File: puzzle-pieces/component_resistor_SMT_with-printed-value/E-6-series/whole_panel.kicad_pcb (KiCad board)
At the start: 2 copper layers, 200 x 200 mm, 175 parts, among them J1 Conn_01x02_Pin, J10 Conn_01x02_Pin, J11 Conn_01x02_Pin, J12 Conn_01x02_Pin, J13 Conn_01x02_Pin, J14 Conn_01x02_Pin, J15 Conn_01x02_Pin, J16 Conn_01x02_Pin, J17 Conn_01x02_Pin, J18 Conn_01x02_Pin, J19 Conn_01x02_Pin, J2 Conn_01x02_Pin, J20 Conn_01x02_Pin, J21 Conn_01x02_Pin, J22 Conn_01x02_Pin, J23 Conn_01x02_Pin, J24 Conn_01x02_Pin, J25 Conn_01x02_Pin, J26 Conn_01x02_Pin, J27 Conn_01x02_Pin, J28 Conn_01x02_Pin, J29 Conn_01x02_Pin, J3 Conn_01x02_Pin, J30 Conn_01x02_Pin, J31 Conn_01x02_Pin, J32 Conn_01x02_Pin, J33 Conn_01x02_Pin, J34 Conn_01x02_Pin, J35 Conn_01x02_Pin, J36 Conn_01x02_Pin, J37 Conn_01x02_Pin, J38 Conn_01x02_Pin, J39 Conn_01x02_Pin, J4 Conn_01x02_Pin, J40 Conn_01x02_Pin, J41 Conn_01x02_Pin, J42 Conn_01x02_Pin, J43 Conn_01x02_Pin, J44 Conn_01x02_Pin, J45 Conn_01x02_Pin, J46 Conn_01x02_Pin, J47 Conn_01x02_Pin, J48 Conn_01x02_Pin, J49 Conn_01x02_Pin, J5 Conn_01x02_Pin, J50 Conn_01x02_Pin, J6 Conn_01x02_Pin, J7 Conn_01x02_Pin, J8 Conn_01x02_Pin, J9 Conn_01x02_Pin

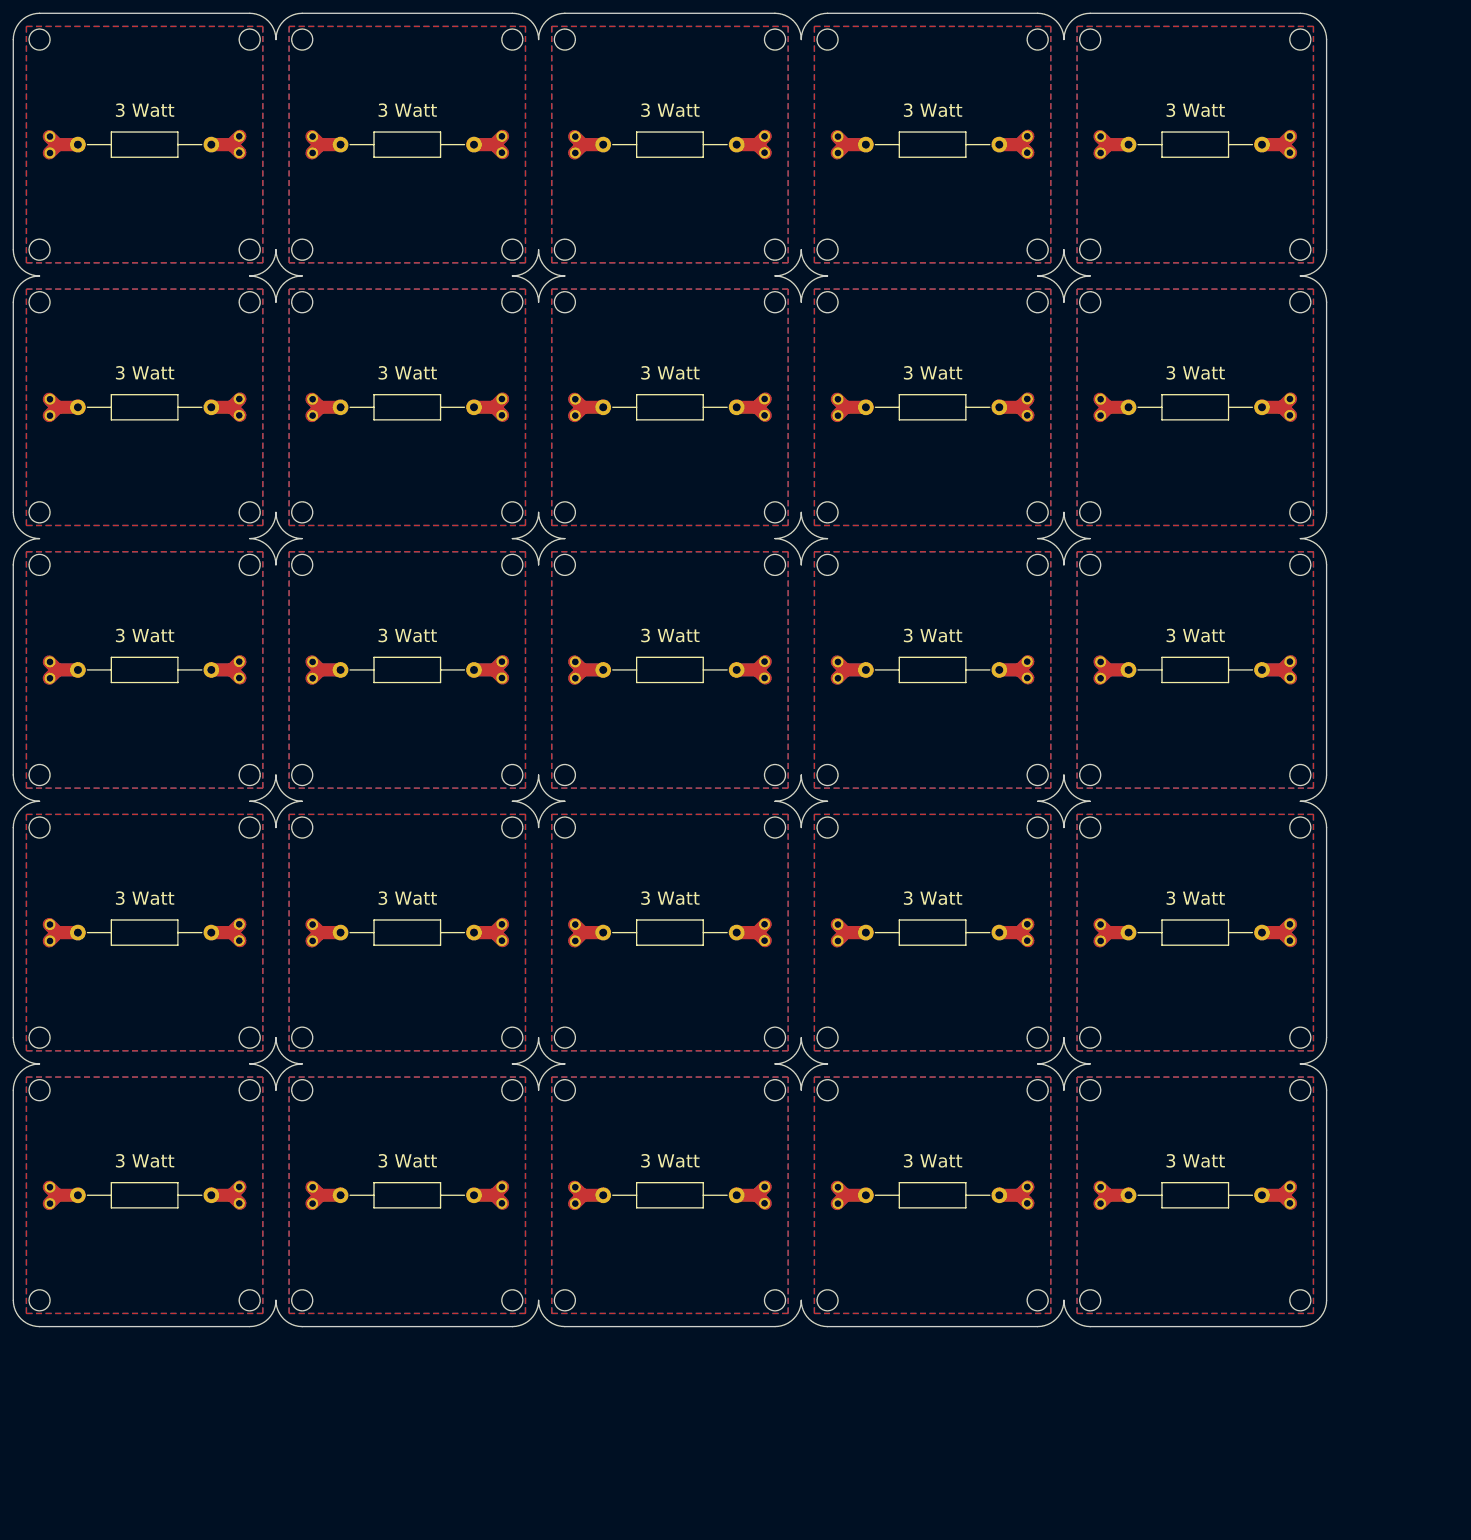
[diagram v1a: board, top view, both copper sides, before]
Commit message: Update resistor footprints and add THT 3W production files
Replaced mounting hole footprints with SMD resistor footprints in the SMT E-6 series panel and updated net assignments. Added new KiCad PCB, project, and production ZIP files for the THT 3W E-6 series resistors. Updated connector reference and position in the SMT panel.
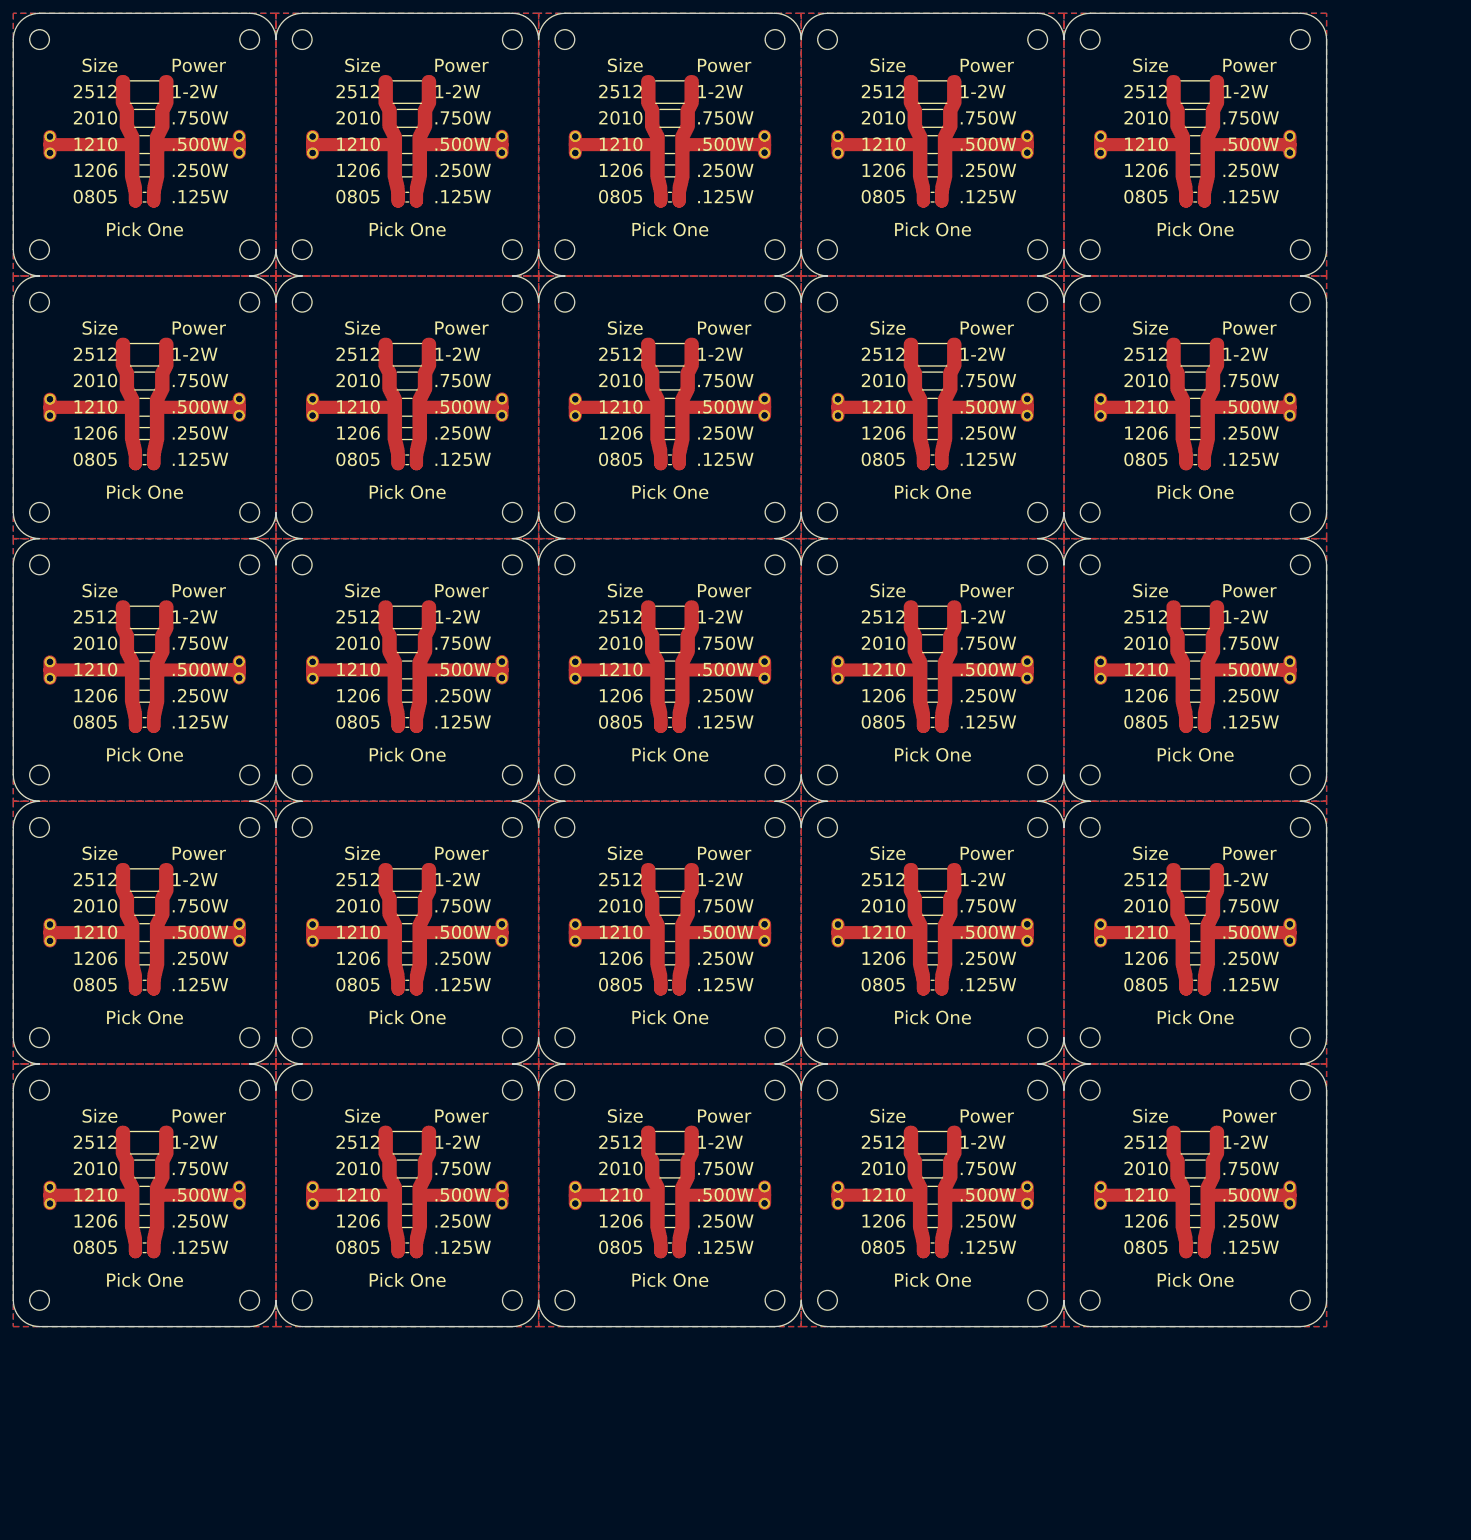
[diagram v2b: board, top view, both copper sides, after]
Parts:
- removed H5 (x100): MH M3, MountingHole:MountingHole_3.2mm_M3
- removed the J1 at (194.5, 180.0)
- removed J10, J11, J12, J13, J14, J15, J16, J17, J18, J19, J20, J21, J22, J23, J24, J25, J26, J27, J28, J29, J3, J30, J31, J32, J33, J34, J35, J36, J37, J38, J39, J4, J40, J41, J42, J43, J44, J45, J46, J47, J48, J49, J5, J50, J6, J7, J8, J9: Conn_01x02_Pin, EASYEDA2KICAD:Magentic_Connector_1x02_P2.5mm_Horizontal
- removed the R1 at (190.2, 180.0)
- removed R10, R11, R12, R13, R14, R15, R16, R17, R18, R19, R20, R21, R22, R23, R24, R25, R6, R7, R8, R9: R, Resistor_THT:R_Axial_DIN0411_L9.9mm_D3.6mm_P20.32mm_Horizontal
- removed the R2 at (30.2, 20.0)
- removed the R3 at (70.2, 20.0)
- removed the R4 at (110.2, 20.0)
- removed the R5 at (150.2, 20.0)
- added H1: MH M3, EASYEDA2KICAD:MountingHole_3.0mm_M3_tight, F.Cu at (156.0, 124.0)
- added H1: MH M3, EASYEDA2KICAD:MountingHole_3.0mm_M3_tight, F.Cu at (156.0, 164.0)
- added H1: MH M3, EASYEDA2KICAD:MountingHole_3.0mm_M3_tight, F.Cu at (116.0, 164.0)
- added H1: MH M3, EASYEDA2KICAD:MountingHole_3.0mm_M3_tight, F.Cu at (76.0, 124.0)
- added H1: MH M3, EASYEDA2KICAD:MountingHole_3.0mm_M3_tight, F.Cu at (76.0, 4.00)
- added H1: MH M3, EASYEDA2KICAD:MountingHole_3.0mm_M3_tight, F.Cu at (36.0, 84.0)
- added H1: MH M3, EASYEDA2KICAD:MountingHole_3.0mm_M3_tight, F.Cu at (36.0, 44.0)
- added H1: MH M3, EASYEDA2KICAD:MountingHole_3.0mm_M3_tight, F.Cu at (156.0, 44.0)
- added H1: MH M3, EASYEDA2KICAD:MountingHole_3.0mm_M3_tight, F.Cu at (196.0, 4.00)
- added H1: MH M3, EASYEDA2KICAD:MountingHole_3.0mm_M3_tight, F.Cu at (196.0, 124.0)
- added H1: MH M3, EASYEDA2KICAD:MountingHole_3.0mm_M3_tight, F.Cu at (196.0, 44.0)
- added H1: MH M3, EASYEDA2KICAD:MountingHole_3.0mm_M3_tight, F.Cu at (116.0, 44.0)
- added H1: MH M3, EASYEDA2KICAD:MountingHole_3.0mm_M3_tight, F.Cu at (116.0, 4.00)
- added H1: MH M3, EASYEDA2KICAD:MountingHole_3.0mm_M3_tight, F.Cu at (156.0, 84.0)
- added H1: MH M3, EASYEDA2KICAD:MountingHole_3.0mm_M3_tight, F.Cu at (116.0, 84.0)
- added H1: MH M3, EASYEDA2KICAD:MountingHole_3.0mm_M3_tight, F.Cu at (196.0, 84.0)
- added H1: MH M3, EASYEDA2KICAD:MountingHole_3.0mm_M3_tight, F.Cu at (196.0, 164.0)
- added H1: MH M3, EASYEDA2KICAD:MountingHole_3.0mm_M3_tight, F.Cu at (156.0, 4.00)
- added H1: MH M3, EASYEDA2KICAD:MountingHole_3.0mm_M3_tight, F.Cu at (116.0, 124.0)
- added H1: MH M3, EASYEDA2KICAD:MountingHole_3.0mm_M3_tight, F.Cu at (76.0, 84.0)
- added H1: MH M3, EASYEDA2KICAD:MountingHole_3.0mm_M3_tight, F.Cu at (36.0, 124.0)
- added H1: MH M3, EASYEDA2KICAD:MountingHole_3.0mm_M3_tight, F.Cu at (76.0, 44.0)
- added H1: MH M3, EASYEDA2KICAD:MountingHole_3.0mm_M3_tight, F.Cu at (76.0, 164.0)
- added H1: MH M3, EASYEDA2KICAD:MountingHole_3.0mm_M3_tight, F.Cu at (36.0, 4.00)
- added H1: MH M3, EASYEDA2KICAD:MountingHole_3.0mm_M3_tight, F.Cu at (36.0, 164.0)
- added H2: MH M3, EASYEDA2KICAD:MountingHole_3.0mm_M3_tight, F.Cu at (4.00, 84.0)
- added H2: MH M3, EASYEDA2KICAD:MountingHole_3.0mm_M3_tight, F.Cu at (124.0, 4.00)
- added H2: MH M3, EASYEDA2KICAD:MountingHole_3.0mm_M3_tight, F.Cu at (124.0, 164.0)
- added H2: MH M3, EASYEDA2KICAD:MountingHole_3.0mm_M3_tight, F.Cu at (124.0, 124.0)
- added H2: MH M3, EASYEDA2KICAD:MountingHole_3.0mm_M3_tight, F.Cu at (164.0, 44.0)
- added H2: MH M3, EASYEDA2KICAD:MountingHole_3.0mm_M3_tight, F.Cu at (84.0, 84.0)
- added H2: MH M3, EASYEDA2KICAD:MountingHole_3.0mm_M3_tight, F.Cu at (84.0, 4.00)
- added H2: MH M3, EASYEDA2KICAD:MountingHole_3.0mm_M3_tight, F.Cu at (44.0, 124.0)
- added H2: MH M3, EASYEDA2KICAD:MountingHole_3.0mm_M3_tight, F.Cu at (44.0, 44.0)
- added H2: MH M3, EASYEDA2KICAD:MountingHole_3.0mm_M3_tight, F.Cu at (44.0, 84.0)
- added H2: MH M3, EASYEDA2KICAD:MountingHole_3.0mm_M3_tight, F.Cu at (84.0, 124.0)
- added H2: MH M3, EASYEDA2KICAD:MountingHole_3.0mm_M3_tight, F.Cu at (4.00, 4.00)
- added H2: MH M3, EASYEDA2KICAD:MountingHole_3.0mm_M3_tight, F.Cu at (124.0, 84.0)
- added H2: MH M3, EASYEDA2KICAD:MountingHole_3.0mm_M3_tight, F.Cu at (124.0, 44.0)
- added H2: MH M3, EASYEDA2KICAD:MountingHole_3.0mm_M3_tight, F.Cu at (4.00, 124.0)
- added H2: MH M3, EASYEDA2KICAD:MountingHole_3.0mm_M3_tight, F.Cu at (164.0, 164.0)
- added H2: MH M3, EASYEDA2KICAD:MountingHole_3.0mm_M3_tight, F.Cu at (4.00, 44.0)
- added H2: MH M3, EASYEDA2KICAD:MountingHole_3.0mm_M3_tight, F.Cu at (164.0, 4.00)
- added H2: MH M3, EASYEDA2KICAD:MountingHole_3.0mm_M3_tight, F.Cu at (164.0, 124.0)
- added H2: MH M3, EASYEDA2KICAD:MountingHole_3.0mm_M3_tight, F.Cu at (84.0, 164.0)
- added H2: MH M3, EASYEDA2KICAD:MountingHole_3.0mm_M3_tight, F.Cu at (84.0, 44.0)
- added H2: MH M3, EASYEDA2KICAD:MountingHole_3.0mm_M3_tight, F.Cu at (164.0, 84.0)
- added H2: MH M3, EASYEDA2KICAD:MountingHole_3.0mm_M3_tight, F.Cu at (4.00, 164.0)
- added H2: MH M3, EASYEDA2KICAD:MountingHole_3.0mm_M3_tight, F.Cu at (44.0, 4.00)
- added H2: MH M3, EASYEDA2KICAD:MountingHole_3.0mm_M3_tight, F.Cu at (44.0, 164.0)
- added H3: MH M3, EASYEDA2KICAD:MountingHole_3.0mm_M3_tight, F.Cu at (156.0, 156.0)
- added H3: MH M3, EASYEDA2KICAD:MountingHole_3.0mm_M3_tight, F.Cu at (156.0, 116.0)
- added H3: MH M3, EASYEDA2KICAD:MountingHole_3.0mm_M3_tight, F.Cu at (196.0, 76.0)
- added H3: MH M3, EASYEDA2KICAD:MountingHole_3.0mm_M3_tight, F.Cu at (36.0, 116.0)
- added H3: MH M3, EASYEDA2KICAD:MountingHole_3.0mm_M3_tight, F.Cu at (76.0, 36.0)
- added H3: MH M3, EASYEDA2KICAD:MountingHole_3.0mm_M3_tight, F.Cu at (36.0, 76.0)
- added H3: MH M3, EASYEDA2KICAD:MountingHole_3.0mm_M3_tight, F.Cu at (196.0, 116.0)
- added H3: MH M3, EASYEDA2KICAD:MountingHole_3.0mm_M3_tight, F.Cu at (116.0, 36.0)
- added H3: MH M3, EASYEDA2KICAD:MountingHole_3.0mm_M3_tight, F.Cu at (116.0, 116.0)
- added H3: MH M3, EASYEDA2KICAD:MountingHole_3.0mm_M3_tight, F.Cu at (36.0, 36.0)
- added H3: MH M3, EASYEDA2KICAD:MountingHole_3.0mm_M3_tight, F.Cu at (156.0, 196.0)
- added H3: MH M3, EASYEDA2KICAD:MountingHole_3.0mm_M3_tight, F.Cu at (196.0, 36.0)
- added H3: MH M3, EASYEDA2KICAD:MountingHole_3.0mm_M3_tight, F.Cu at (76.0, 156.0)
- added H3: MH M3, EASYEDA2KICAD:MountingHole_3.0mm_M3_tight, F.Cu at (76.0, 196.0)
- added H3: MH M3, EASYEDA2KICAD:MountingHole_3.0mm_M3_tight, F.Cu at (196.0, 196.0)
- added H3: MH M3, EASYEDA2KICAD:MountingHole_3.0mm_M3_tight, F.Cu at (76.0, 76.0)
- added H3: MH M3, EASYEDA2KICAD:MountingHole_3.0mm_M3_tight, F.Cu at (116.0, 156.0)
- added H3: MH M3, EASYEDA2KICAD:MountingHole_3.0mm_M3_tight, F.Cu at (36.0, 196.0)
- added H3: MH M3, EASYEDA2KICAD:MountingHole_3.0mm_M3_tight, F.Cu at (116.0, 76.0)
- added H3: MH M3, EASYEDA2KICAD:MountingHole_3.0mm_M3_tight, F.Cu at (156.0, 76.0)
- added H3: MH M3, EASYEDA2KICAD:MountingHole_3.0mm_M3_tight, F.Cu at (116.0, 196.0)
- added H3: MH M3, EASYEDA2KICAD:MountingHole_3.0mm_M3_tight, F.Cu at (36.0, 156.0)
- added H3: MH M3, EASYEDA2KICAD:MountingHole_3.0mm_M3_tight, F.Cu at (76.0, 116.0)
- added H3: MH M3, EASYEDA2KICAD:MountingHole_3.0mm_M3_tight, F.Cu at (196.0, 156.0)
- added H3: MH M3, EASYEDA2KICAD:MountingHole_3.0mm_M3_tight, F.Cu at (156.0, 36.0)
- added H4: MH M3, EASYEDA2KICAD:MountingHole_3.0mm_M3_tight, F.Cu at (84.0, 196.0)
- added H4: MH M3, EASYEDA2KICAD:MountingHole_3.0mm_M3_tight, F.Cu at (44.0, 196.0)
- added H4: MH M3, EASYEDA2KICAD:MountingHole_3.0mm_M3_tight, F.Cu at (4.00, 76.0)
- added H4: MH M3, EASYEDA2KICAD:MountingHole_3.0mm_M3_tight, F.Cu at (124.0, 196.0)
- added H4: MH M3, EASYEDA2KICAD:MountingHole_3.0mm_M3_tight, F.Cu at (84.0, 76.0)
- added H4: MH M3, EASYEDA2KICAD:MountingHole_3.0mm_M3_tight, F.Cu at (124.0, 116.0)
- added H4: MH M3, EASYEDA2KICAD:MountingHole_3.0mm_M3_tight, F.Cu at (84.0, 116.0)
- added H4: MH M3, EASYEDA2KICAD:MountingHole_3.0mm_M3_tight, F.Cu at (4.00, 156.0)
- added H4: MH M3, EASYEDA2KICAD:MountingHole_3.0mm_M3_tight, F.Cu at (124.0, 36.0)
- added H4: MH M3, EASYEDA2KICAD:MountingHole_3.0mm_M3_tight, F.Cu at (164.0, 156.0)
- added H4: MH M3, EASYEDA2KICAD:MountingHole_3.0mm_M3_tight, F.Cu at (84.0, 36.0)
- added H4: MH M3, EASYEDA2KICAD:MountingHole_3.0mm_M3_tight, F.Cu at (164.0, 36.0)
- added H4: MH M3, EASYEDA2KICAD:MountingHole_3.0mm_M3_tight, F.Cu at (164.0, 196.0)
- added H4: MH M3, EASYEDA2KICAD:MountingHole_3.0mm_M3_tight, F.Cu at (164.0, 116.0)
- added H4: MH M3, EASYEDA2KICAD:MountingHole_3.0mm_M3_tight, F.Cu at (4.00, 36.0)
- added H4: MH M3, EASYEDA2KICAD:MountingHole_3.0mm_M3_tight, F.Cu at (84.0, 156.0)
- added H4: MH M3, EASYEDA2KICAD:MountingHole_3.0mm_M3_tight, F.Cu at (44.0, 116.0)
- added H4: MH M3, EASYEDA2KICAD:MountingHole_3.0mm_M3_tight, F.Cu at (4.00, 116.0)
- added H4: MH M3, EASYEDA2KICAD:MountingHole_3.0mm_M3_tight, F.Cu at (124.0, 76.0)
- added H4: MH M3, EASYEDA2KICAD:MountingHole_3.0mm_M3_tight, F.Cu at (124.0, 156.0)
- added H4: MH M3, EASYEDA2KICAD:MountingHole_3.0mm_M3_tight, F.Cu at (4.00, 196.0)
- added H4: MH M3, EASYEDA2KICAD:MountingHole_3.0mm_M3_tight, F.Cu at (44.0, 156.0)
- added H4: MH M3, EASYEDA2KICAD:MountingHole_3.0mm_M3_tight, F.Cu at (44.0, 36.0)
- added H4: MH M3, EASYEDA2KICAD:MountingHole_3.0mm_M3_tight, F.Cu at (44.0, 76.0)
- added H4: MH M3, EASYEDA2KICAD:MountingHole_3.0mm_M3_tight, F.Cu at (164.0, 76.0)
- added J1: Conn_01x02_Pin, EASYEDA2KICAD:Magentic_Connector_1x02_P2.5mm_Horizontal, F.Cu at (45.5, 60.0)
- added J1: Conn_01x02_Pin, EASYEDA2KICAD:Magentic_Connector_1x02_P2.5mm_Horizontal, F.Cu at (5.49, 180.0)
- added J1: Conn_01x02_Pin, EASYEDA2KICAD:Magentic_Connector_1x02_P2.5mm_Horizontal, F.Cu at (125.5, 100.0)
- added J1: Conn_01x02_Pin, EASYEDA2KICAD:Magentic_Connector_1x02_P2.5mm_Horizontal, F.Cu at (165.5, 20.0)
- added J1: Conn_01x02_Pin, EASYEDA2KICAD:Magentic_Connector_1x02_P2.5mm_Horizontal, F.Cu at (45.5, 20.0)
- added J1: Conn_01x02_Pin, EASYEDA2KICAD:Magentic_Connector_1x02_P2.5mm_Horizontal, F.Cu at (85.5, 180.0)
- added J1: Conn_01x02_Pin, EASYEDA2KICAD:Magentic_Connector_1x02_P2.5mm_Horizontal, F.Cu at (45.5, 180.0)
- added J1: Conn_01x02_Pin, EASYEDA2KICAD:Magentic_Connector_1x02_P2.5mm_Horizontal, F.Cu at (5.49, 60.0)
- added J1: Conn_01x02_Pin, EASYEDA2KICAD:Magentic_Connector_1x02_P2.5mm_Horizontal, F.Cu at (85.5, 140.0)
- added J1: Conn_01x02_Pin, EASYEDA2KICAD:Magentic_Connector_1x02_P2.5mm_Horizontal, F.Cu at (85.5, 20.0)
- added J1: Conn_01x02_Pin, EASYEDA2KICAD:Magentic_Connector_1x02_P2.5mm_Horizontal, F.Cu at (165.5, 180.0)
- added J1: Conn_01x02_Pin, EASYEDA2KICAD:Magentic_Connector_1x02_P2.5mm_Horizontal, F.Cu at (165.5, 100.0)
- added J1: Conn_01x02_Pin, EASYEDA2KICAD:Magentic_Connector_1x02_P2.5mm_Horizontal, F.Cu at (125.5, 180.0)
- added J1: Conn_01x02_Pin, EASYEDA2KICAD:Magentic_Connector_1x02_P2.5mm_Horizontal, F.Cu at (85.5, 100.0)
- added J1: Conn_01x02_Pin, EASYEDA2KICAD:Magentic_Connector_1x02_P2.5mm_Horizontal, F.Cu at (45.5, 100.0)
- added J1: Conn_01x02_Pin, EASYEDA2KICAD:Magentic_Connector_1x02_P2.5mm_Horizontal, F.Cu at (5.49, 140.0)
- added J1: Conn_01x02_Pin, EASYEDA2KICAD:Magentic_Connector_1x02_P2.5mm_Horizontal, F.Cu at (45.5, 140.0)
- added J1: Conn_01x02_Pin, EASYEDA2KICAD:Magentic_Connector_1x02_P2.5mm_Horizontal, F.Cu at (5.49, 20.0)
- added J1: Conn_01x02_Pin, EASYEDA2KICAD:Magentic_Connector_1x02_P2.5mm_Horizontal, F.Cu at (125.5, 60.0)
- added J1: Conn_01x02_Pin, EASYEDA2KICAD:Magentic_Connector_1x02_P2.5mm_Horizontal, F.Cu at (165.5, 140.0)
- added J1: Conn_01x02_Pin, EASYEDA2KICAD:Magentic_Connector_1x02_P2.5mm_Horizontal, F.Cu at (125.5, 20.0)
- added J1: Conn_01x02_Pin, EASYEDA2KICAD:Magentic_Connector_1x02_P2.5mm_Horizontal, F.Cu at (85.5, 60.0)
- added J1: Conn_01x02_Pin, EASYEDA2KICAD:Magentic_Connector_1x02_P2.5mm_Horizontal, F.Cu at (165.5, 60.0)
- added J1: Conn_01x02_Pin, EASYEDA2KICAD:Magentic_Connector_1x02_P2.5mm_Horizontal, F.Cu at (5.49, 100.0)
- added J1: Conn_01x02_Pin, EASYEDA2KICAD:Magentic_Connector_1x02_P2.5mm_Horizontal, F.Cu at (125.5, 140.0)
- added J2: Conn_01x02_Pin, EASYEDA2KICAD:Magentic_Connector_1x02_P2.5mm_Horizontal, F.Cu at (34.5, 140.0)
- added J2: Conn_01x02_Pin, EASYEDA2KICAD:Magentic_Connector_1x02_P2.5mm_Horizontal, F.Cu at (114.5, 20.0)
- added J2: Conn_01x02_Pin, EASYEDA2KICAD:Magentic_Connector_1x02_P2.5mm_Horizontal, F.Cu at (154.5, 140.0)
- added J2: Conn_01x02_Pin, EASYEDA2KICAD:Magentic_Connector_1x02_P2.5mm_Horizontal, F.Cu at (114.5, 100.0)
- added J2: Conn_01x02_Pin, EASYEDA2KICAD:Magentic_Connector_1x02_P2.5mm_Horizontal, F.Cu at (114.5, 180.0)
- added J2: Conn_01x02_Pin, EASYEDA2KICAD:Magentic_Connector_1x02_P2.5mm_Horizontal, F.Cu at (194.5, 20.0)
- added J2: Conn_01x02_Pin, EASYEDA2KICAD:Magentic_Connector_1x02_P2.5mm_Horizontal, F.Cu at (114.5, 140.0)
- added J2: Conn_01x02_Pin, EASYEDA2KICAD:Magentic_Connector_1x02_P2.5mm_Horizontal, F.Cu at (34.5, 100.0)
- added J2: Conn_01x02_Pin, EASYEDA2KICAD:Magentic_Connector_1x02_P2.5mm_Horizontal, F.Cu at (194.5, 100.0)
- added J2: Conn_01x02_Pin, EASYEDA2KICAD:Magentic_Connector_1x02_P2.5mm_Horizontal, F.Cu at (194.5, 60.0)
- added J2: Conn_01x02_Pin, EASYEDA2KICAD:Magentic_Connector_1x02_P2.5mm_Horizontal, F.Cu at (74.5, 100.0)
- added J2: Conn_01x02_Pin, EASYEDA2KICAD:Magentic_Connector_1x02_P2.5mm_Horizontal, F.Cu at (74.5, 20.0)
- added J2: Conn_01x02_Pin, EASYEDA2KICAD:Magentic_Connector_1x02_P2.5mm_Horizontal, F.Cu at (74.5, 60.0)
- added J2: Conn_01x02_Pin, EASYEDA2KICAD:Magentic_Connector_1x02_P2.5mm_Horizontal, F.Cu at (194.5, 180.0)
- added J2: Conn_01x02_Pin, EASYEDA2KICAD:Magentic_Connector_1x02_P2.5mm_Horizontal, F.Cu at (74.5, 180.0)
- added J2: Conn_01x02_Pin, EASYEDA2KICAD:Magentic_Connector_1x02_P2.5mm_Horizontal, F.Cu at (74.5, 140.0)
- added J2: Conn_01x02_Pin, EASYEDA2KICAD:Magentic_Connector_1x02_P2.5mm_Horizontal, F.Cu at (154.5, 180.0)
- added J2: Conn_01x02_Pin, EASYEDA2KICAD:Magentic_Connector_1x02_P2.5mm_Horizontal, F.Cu at (194.5, 140.0)
- added J2: Conn_01x02_Pin, EASYEDA2KICAD:Magentic_Connector_1x02_P2.5mm_Horizontal, F.Cu at (34.5, 60.0)
- added J2: Conn_01x02_Pin, EASYEDA2KICAD:Magentic_Connector_1x02_P2.5mm_Horizontal, F.Cu at (154.5, 60.0)
- added J2: Conn_01x02_Pin, EASYEDA2KICAD:Magentic_Connector_1x02_P2.5mm_Horizontal, F.Cu at (154.5, 20.0)
- added J2: Conn_01x02_Pin, EASYEDA2KICAD:Magentic_Connector_1x02_P2.5mm_Horizontal, F.Cu at (34.5, 180.0)
- added J2: Conn_01x02_Pin, EASYEDA2KICAD:Magentic_Connector_1x02_P2.5mm_Horizontal, F.Cu at (114.5, 60.0)
- added J2: Conn_01x02_Pin, EASYEDA2KICAD:Magentic_Connector_1x02_P2.5mm_Horizontal, F.Cu at (154.5, 100.0)
- added R1: R, Resistor_SMD:R_2512_6332Metric, F.Cu at (60.0, 132.0)
- added R1: R, Resistor_SMD:R_2512_6332Metric, F.Cu at (20.0, 172.0)
- added R1: R, Resistor_SMD:R_2512_6332Metric, F.Cu at (180.0, 172.0)
- added R1: R, Resistor_SMD:R_2512_6332Metric, F.Cu at (20.0, 52.0)
- added R1: R, Resistor_SMD:R_2512_6332Metric, F.Cu at (100.0, 92.0)
- added R1: R, Resistor_SMD:R_2512_6332Metric, F.Cu at (180.0, 52.0)
- added R1: R, Resistor_SMD:R_2512_6332Metric, F.Cu at (140.0, 132.0)
- added R1: R, Resistor_SMD:R_2512_6332Metric, F.Cu at (100.0, 172.0)
- added R1: R, Resistor_SMD:R_2512_6332Metric, F.Cu at (180.0, 132.0)
- added R1: R, Resistor_SMD:R_2512_6332Metric, F.Cu at (60.0, 52.0)
- added R1: R, Resistor_SMD:R_2512_6332Metric, F.Cu at (20.0, 132.0)
- added R1: R, Resistor_SMD:R_2512_6332Metric, F.Cu at (140.0, 172.0)
- added R1: R, Resistor_SMD:R_2512_6332Metric, F.Cu at (100.0, 12.0)
- added R1: R, Resistor_SMD:R_2512_6332Metric, F.Cu at (140.0, 12.0)
- added R1: R, Resistor_SMD:R_2512_6332Metric, F.Cu at (180.0, 12.0)
- added R1: R, Resistor_SMD:R_2512_6332Metric, F.Cu at (60.0, 12.0)
- added R1: R, Resistor_SMD:R_2512_6332Metric, F.Cu at (180.0, 92.0)
- added R1: R, Resistor_SMD:R_2512_6332Metric, F.Cu at (20.0, 92.0)
- added R1: R, Resistor_SMD:R_2512_6332Metric, F.Cu at (100.0, 132.0)
- added R1: R, Resistor_SMD:R_2512_6332Metric, F.Cu at (20.0, 12.0)
- added R1: R, Resistor_SMD:R_2512_6332Metric, F.Cu at (60.0, 172.0)
- added R1: R, Resistor_SMD:R_2512_6332Metric, F.Cu at (140.0, 92.0)
- added R1: R, Resistor_SMD:R_2512_6332Metric, F.Cu at (100.0, 52.0)
- added R1: R, Resistor_SMD:R_2512_6332Metric, F.Cu at (60.0, 92.0)
- added R1: R, Resistor_SMD:R_2512_6332Metric, F.Cu at (140.0, 52.0)
- added R2: R, Resistor_SMD:R_2010_5025Metric, F.Cu at (100.0, 16.0)
- added R2: R, Resistor_SMD:R_2010_5025Metric, F.Cu at (20.0, 16.0)
- added R2: R, Resistor_SMD:R_2010_5025Metric, F.Cu at (140.0, 136.0)
- added R2: R, Resistor_SMD:R_2010_5025Metric, F.Cu at (140.0, 56.0)
- added R2: R, Resistor_SMD:R_2010_5025Metric, F.Cu at (180.0, 176.0)
- added R2: R, Resistor_SMD:R_2010_5025Metric, F.Cu at (180.0, 56.0)
- added R2: R, Resistor_SMD:R_2010_5025Metric, F.Cu at (20.0, 136.0)
- added R2: R, Resistor_SMD:R_2010_5025Metric, F.Cu at (60.0, 136.0)
- added R2: R, Resistor_SMD:R_2010_5025Metric, F.Cu at (60.0, 56.0)
- added R2: R, Resistor_SMD:R_2010_5025Metric, F.Cu at (100.0, 96.0)
- added R2: R, Resistor_SMD:R_2010_5025Metric, F.Cu at (180.0, 16.0)
- added R2: R, Resistor_SMD:R_2010_5025Metric, F.Cu at (20.0, 176.0)
- added R2: R, Resistor_SMD:R_2010_5025Metric, F.Cu at (20.0, 96.0)
- added R2: R, Resistor_SMD:R_2010_5025Metric, F.Cu at (140.0, 96.0)
- added R2: R, Resistor_SMD:R_2010_5025Metric, F.Cu at (100.0, 56.0)
- added R2: R, Resistor_SMD:R_2010_5025Metric, F.Cu at (140.0, 176.0)
- added R2: R, Resistor_SMD:R_2010_5025Metric, F.Cu at (60.0, 176.0)
- added R2: R, Resistor_SMD:R_2010_5025Metric, F.Cu at (180.0, 136.0)
- added R2: R, Resistor_SMD:R_2010_5025Metric, F.Cu at (60.0, 16.0)
- added R2: R, Resistor_SMD:R_2010_5025Metric, F.Cu at (180.0, 96.0)
- added R2: R, Resistor_SMD:R_2010_5025Metric, F.Cu at (140.0, 16.0)
- added R2: R, Resistor_SMD:R_2010_5025Metric, F.Cu at (60.0, 96.0)
- added R2: R, Resistor_SMD:R_2010_5025Metric, F.Cu at (20.0, 56.0)
- added R2: R, Resistor_SMD:R_2010_5025Metric, F.Cu at (100.0, 176.0)
- added R2: R, Resistor_SMD:R_2010_5025Metric, F.Cu at (100.0, 136.0)
- added R3: R, Resistor_SMD:R_1210_3225Metric, F.Cu at (60.0, 140.0)
- added R3: R, Resistor_SMD:R_1210_3225Metric, F.Cu at (100.0, 180.0)
- added R3: R, Resistor_SMD:R_1210_3225Metric, F.Cu at (140.0, 20.0)
- added R3: R, Resistor_SMD:R_1210_3225Metric, F.Cu at (100.0, 100.0)
- added R3: R, Resistor_SMD:R_1210_3225Metric, F.Cu at (20.0, 180.0)
- added R3: R, Resistor_SMD:R_1210_3225Metric, F.Cu at (180.0, 140.0)
- added R3: R, Resistor_SMD:R_1210_3225Metric, F.Cu at (180.0, 60.0)
- added R3: R, Resistor_SMD:R_1210_3225Metric, F.Cu at (60.0, 100.0)
- added R3: R, Resistor_SMD:R_1210_3225Metric, F.Cu at (100.0, 20.0)
- added R3: R, Resistor_SMD:R_1210_3225Metric, F.Cu at (60.0, 180.0)
- added R3: R, Resistor_SMD:R_1210_3225Metric, F.Cu at (180.0, 180.0)
- added R3: R, Resistor_SMD:R_1210_3225Metric, F.Cu at (60.0, 20.0)
- added R3: R, Resistor_SMD:R_1210_3225Metric, F.Cu at (140.0, 180.0)
- added R3: R, Resistor_SMD:R_1210_3225Metric, F.Cu at (20.0, 140.0)
- added R3: R, Resistor_SMD:R_1210_3225Metric, F.Cu at (100.0, 60.0)
- added R3: R, Resistor_SMD:R_1210_3225Metric, F.Cu at (180.0, 100.0)
- added R3: R, Resistor_SMD:R_1210_3225Metric, F.Cu at (140.0, 60.0)
- added R3: R, Resistor_SMD:R_1210_3225Metric, F.Cu at (60.0, 60.0)
- added R3: R, Resistor_SMD:R_1210_3225Metric, F.Cu at (100.0, 140.0)
- added R3: R, Resistor_SMD:R_1210_3225Metric, F.Cu at (140.0, 140.0)
- added R3: R, Resistor_SMD:R_1210_3225Metric, F.Cu at (140.0, 100.0)
- added R3: R, Resistor_SMD:R_1210_3225Metric, F.Cu at (20.0, 20.0)
- added R3: R, Resistor_SMD:R_1210_3225Metric, F.Cu at (20.0, 60.0)
- added R3: R, Resistor_SMD:R_1210_3225Metric, F.Cu at (20.0, 100.0)
- added R3: R, Resistor_SMD:R_1210_3225Metric, F.Cu at (180.0, 20.0)
- added R4: R, Resistor_SMD:R_1206_3216Metric, F.Cu at (180.0, 144.0)
- added R4: R, Resistor_SMD:R_1206_3216Metric, F.Cu at (60.0, 184.0)
- added R4: R, Resistor_SMD:R_1206_3216Metric, F.Cu at (180.0, 64.0)
- added R4: R, Resistor_SMD:R_1206_3216Metric, F.Cu at (20.0, 24.0)
- added R4: R, Resistor_SMD:R_1206_3216Metric, F.Cu at (100.0, 24.0)
- added R4: R, Resistor_SMD:R_1206_3216Metric, F.Cu at (140.0, 184.0)
- added R4: R, Resistor_SMD:R_1206_3216Metric, F.Cu at (20.0, 104.0)
- added R4: R, Resistor_SMD:R_1206_3216Metric, F.Cu at (100.0, 184.0)
- added R4: R, Resistor_SMD:R_1206_3216Metric, F.Cu at (180.0, 24.0)
- added R4: R, Resistor_SMD:R_1206_3216Metric, F.Cu at (140.0, 24.0)
- added R4: R, Resistor_SMD:R_1206_3216Metric, F.Cu at (60.0, 64.0)
- added R4: R, Resistor_SMD:R_1206_3216Metric, F.Cu at (60.0, 144.0)
- added R4: R, Resistor_SMD:R_1206_3216Metric, F.Cu at (180.0, 184.0)
- added R4: R, Resistor_SMD:R_1206_3216Metric, F.Cu at (100.0, 64.0)
- added R4: R, Resistor_SMD:R_1206_3216Metric, F.Cu at (20.0, 144.0)
- added R4: R, Resistor_SMD:R_1206_3216Metric, F.Cu at (20.0, 64.0)
- added R4: R, Resistor_SMD:R_1206_3216Metric, F.Cu at (60.0, 24.0)
- added R4: R, Resistor_SMD:R_1206_3216Metric, F.Cu at (60.0, 104.0)
- added R4: R, Resistor_SMD:R_1206_3216Metric, F.Cu at (100.0, 104.0)
- added R4: R, Resistor_SMD:R_1206_3216Metric, F.Cu at (100.0, 144.0)
- added R4: R, Resistor_SMD:R_1206_3216Metric, F.Cu at (140.0, 64.0)
- added R4: R, Resistor_SMD:R_1206_3216Metric, F.Cu at (180.0, 104.0)
- added R4: R, Resistor_SMD:R_1206_3216Metric, F.Cu at (140.0, 104.0)
- added R4: R, Resistor_SMD:R_1206_3216Metric, F.Cu at (20.0, 184.0)
- added R4: R, Resistor_SMD:R_1206_3216Metric, F.Cu at (140.0, 144.0)
- added R5: R, Resistor_SMD:R_0805_2012Metric, F.Cu at (140.0, 148.0)
- added R5: R, Resistor_SMD:R_0805_2012Metric, F.Cu at (60.0, 188.0)
- added R5: R, Resistor_SMD:R_0805_2012Metric, F.Cu at (60.0, 148.0)
- added R5: R, Resistor_SMD:R_0805_2012Metric, F.Cu at (180.0, 108.0)
- added R5: R, Resistor_SMD:R_0805_2012Metric, F.Cu at (180.0, 188.0)
- added R5: R, Resistor_SMD:R_0805_2012Metric, F.Cu at (60.0, 108.0)
- added R5: R, Resistor_SMD:R_0805_2012Metric, F.Cu at (100.0, 108.0)
- added R5: R, Resistor_SMD:R_0805_2012Metric, F.Cu at (100.0, 68.0)
- added R5: R, Resistor_SMD:R_0805_2012Metric, F.Cu at (140.0, 108.0)
- added R5: R, Resistor_SMD:R_0805_2012Metric, F.Cu at (60.0, 68.0)
- added R5: R, Resistor_SMD:R_0805_2012Metric, F.Cu at (100.0, 28.0)
- added R5: R, Resistor_SMD:R_0805_2012Metric, F.Cu at (20.0, 188.0)
- added R5: R, Resistor_SMD:R_0805_2012Metric, F.Cu at (180.0, 28.0)
- added R5: R, Resistor_SMD:R_0805_2012Metric, F.Cu at (180.0, 148.0)
- added R5: R, Resistor_SMD:R_0805_2012Metric, F.Cu at (20.0, 68.0)
- added R5: R, Resistor_SMD:R_0805_2012Metric, F.Cu at (140.0, 28.0)
- added R5: R, Resistor_SMD:R_0805_2012Metric, F.Cu at (140.0, 188.0)
- added R5: R, Resistor_SMD:R_0805_2012Metric, F.Cu at (20.0, 148.0)
- added R5: R, Resistor_SMD:R_0805_2012Metric, F.Cu at (20.0, 108.0)
- added R5: R, Resistor_SMD:R_0805_2012Metric, F.Cu at (100.0, 148.0)
- added R5: R, Resistor_SMD:R_0805_2012Metric, F.Cu at (20.0, 28.0)
- added R5: R, Resistor_SMD:R_0805_2012Metric, F.Cu at (140.0, 68.0)
- added R5: R, Resistor_SMD:R_0805_2012Metric, F.Cu at (180.0, 68.0)
- added R5: R, Resistor_SMD:R_0805_2012Metric, F.Cu at (60.0, 28.0)
- added R5: R, Resistor_SMD:R_0805_2012Metric, F.Cu at (100.0, 188.0)
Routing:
- net Net-(J2-Pin_1): track 166.5 -> 401.1 mm
- net NordSued: track 165.5 -> 390.0 mm
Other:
- board text added: ".125W"
- board text added: ".250W"
- board text added: ".500W"
- board text added: ".750W"
- board text added: "0805"
- board text added: "1-2W"
- board text added: "1206"
- board text added: "1210"
- board text added: "2010"
- board text added: "2512"
- board text added: "Pick One"
- board text added: "Power"
- board text added: "Size"
- board text removed: "3 Watt"
